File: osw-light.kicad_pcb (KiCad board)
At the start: 2 copper layers, 34.9 x 36.2 mm, 56 parts, among them J1 Conn_01x02, J2 USB_C_Receptacle_USB2.0, J3 Conn_01x02, J4 Conn_01x04, J5 Conn_01x04, Q1 2N7002, SW1 SW_Push, SW2 SW_Push, SW4 SW_Push, SW5 SW_Push, U1 DS3231MZ, U10 XC6209, U11 MCP73831T-2ACI_OT, U13 XC6209, U2 BMA400, U4 GC9A01_IPS_display, U6 CH340E, U7 ttgo-32-micro, U9 TPS2115A

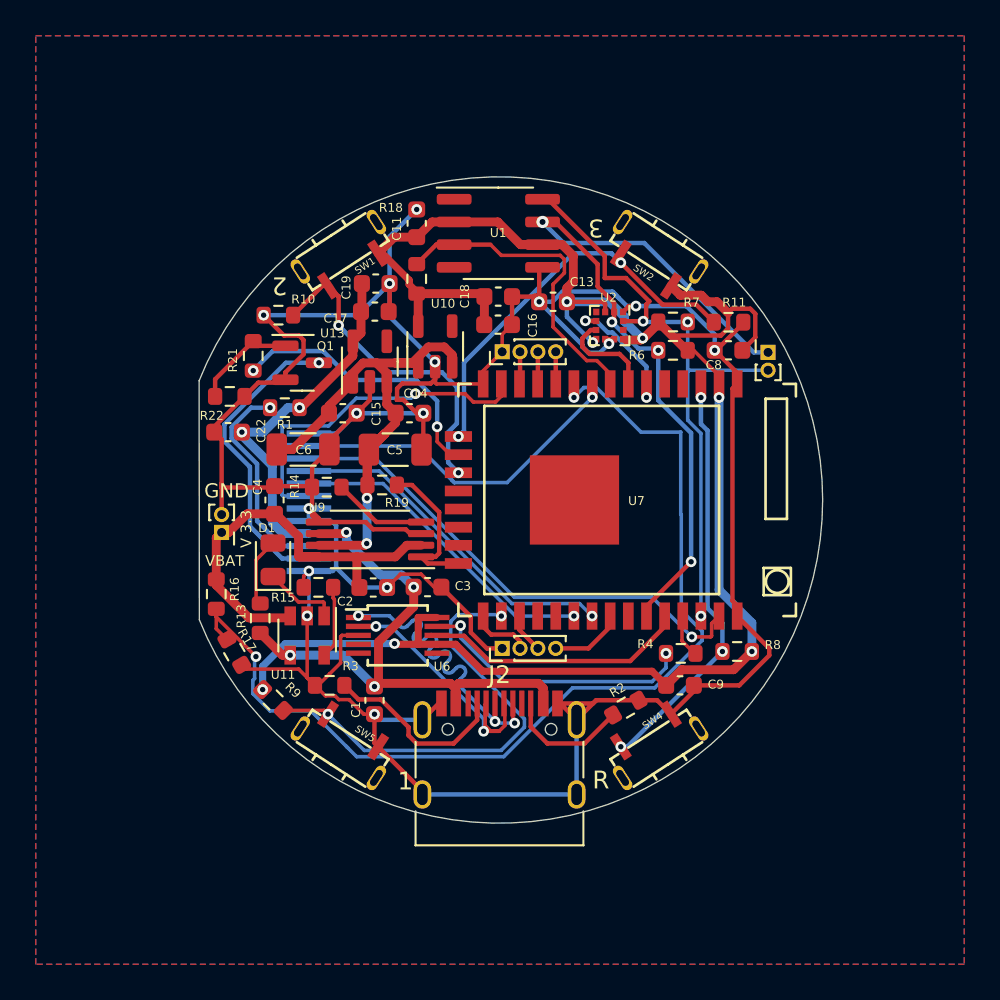
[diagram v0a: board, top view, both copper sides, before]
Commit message: re-thought some aspects of the pcb and schematics: now there is only one ldo and pcb layout is now better for hand soldering, still needs some cleanup (and bom consolidation)
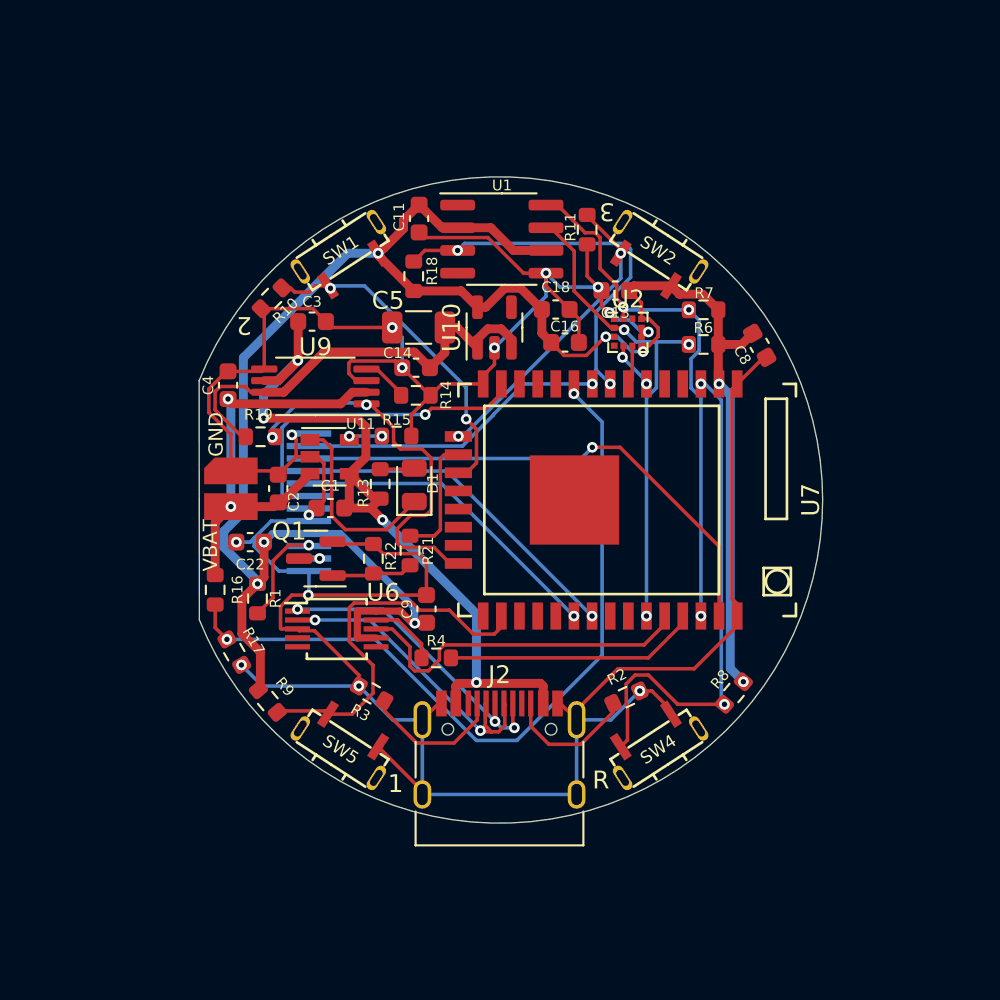
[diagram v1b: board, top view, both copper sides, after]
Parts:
- removed C15, C19: 0.1u, Capacitor_SMD:C_0603_1608Metric
- removed C17: 4.7u, Capacitor_SMD:C_0603_1608Metric
- removed C6: 100u, Capacitor_SMD:C_1206_3216Metric
- removed J3: Conn_01x02, open-Smartwatch:PinHeader_1x02_P1.0mm_Vertical
- removed J4, J5: Conn_01x04, open-Smartwatch:PinHeader_1x04_P1.00mm_Vertical
- removed U13: XC6209, Package_TO_SOT_SMD:SOT-23-5
- J1: footprint open-Smartwatch:PinHeader_1x02_P1.0mm_Vertical -> open-Smartwatch:batteryPads
- moved C3 16.2 mm to (58.5, 102.0)
- moved C9 14.8 mm to (64.9, 118.1), turned to 90 degrees
- moved R21 14.0 mm to (64.0, 114.8), turned to 90 degrees
- moved R4 13.7 mm to (65.4, 120.8)
- moved R22 12.1 mm to (61.9, 115.3), turned to -90 degrees
- moved C1 11.0 mm to (59.5, 112.5), turned to 0 degrees
- moved Q1 11.0 mm to (58.7, 115.3), turned to 180 degrees
- moved R1 10.8 mm to (55.4, 117.5), turned to -90 degrees
- moved U11 10.1 mm to (59.5, 109.6), turned to 0 degrees
- moved R13 10.1 mm to (62.3, 111.1)
- moved R15 9.53 mm to (63.2, 108.4), turned to 0 degrees
- moved R11 9.46 mm to (73.9, 96.9), turned to -90 degrees
- moved U9 9.10 mm to (58.7, 105.6)
- moved D1 8.95 mm to (64.2, 111.2)
- moved C2 7.68 mm to (56.6, 111.4), turned to 90 degrees
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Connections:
- net /VBUS renamed VBUS
- net /VCC renamed VCC
- net Net-(D1-Pad1) renamed /STAT
- net Net-(Q1-Pad1) renamed /GATE
- net Net-(R1-Pad2) renamed /LEDA
- net Net-(R14-Pad1) renamed /ILIM
- net Net-(R15-Pad1) renamed /PROG
- C22 pad 1: /3V3_2 -> +3V3
- J1 pad 1: /VBAT -> GND
- J1 pad 2: GND -> /VBAT
- R1 pad 1: /3V3_2 -> +3V3
- U4 pad 4: /3V3_2 -> +3V3
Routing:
- net /3V3_2: track 20.3 -> 0.00 mm, vias 2 -> 0
- net GND: track 202.4 -> 182.1 mm, vias 15 -> 14
- net /SDA: track 43.9 -> 27.6 mm, vias 4 -> 3
- net /LEDK: track 17.1 -> 1.15 mm
- net /B_MON: track 57.3 -> 42.9 mm
- net /STAT_PWR: track 8.63 -> 21.9 mm, vias 0 -> 2
- net Net-(R4-Pad1): track 15.7 -> 3.89 mm, vias 2 -> 0
- net /TX: track 2.48 -> 14.2 mm
- net VCC: track 36.7 -> 25.2 mm, vias 2 -> 0
- net +3V3: track 107.8 -> 117.9 mm, vias 7 -> 8
- net VBUS: track 33.5 -> 43.3 mm
- net /PIN_LED: track 15.7 -> 6.93 mm, vias 2 -> 0
- net /STAT: track 4.20 -> 10.8 mm
- net /LEDA: track 11.9 -> 5.67 mm
- net /BTN3: track 22.4 -> 17.0 mm
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- removed copper zone on B.Cu, net GND
- removed copper zone on F.Cu, net GND
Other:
- board text removed: "GND"
- board text removed: "V 3.3"
- board text removed: "VBAT"

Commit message: pcb cleanup
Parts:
- R16: value 200k -> 210k
- R19: value 220k -> 210k
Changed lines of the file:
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@@
       (effects (font (size 0.6 0.6) (thickness 0.09)))
     )
-    (fp_text value "220k" (at 0 1.43) (layer "F.Fab")
+    (fp_text value "210k" (at 0 1.43) (layer "F.Fab")
       (effects (font (size 1 1) (thickness 0.15)))
     )
@@
     (property "Sheetname" "")
     (attr smd)
-    (fp_text reference "R13" (at 0.51 0.94 -90) (layer "F.SilkS")
+    (fp_text reference "R13" (at 0.68 0.95 -90) (layer "F.SilkS")
       (effects (font (size 0.6 0.6) (thickness 0.09)))
     )
@@
     (property "Sheetname" "")
     (attr smd)
-    (fp_text reference "U10" (at 0 -2.4 90) (layer "F.SilkS")
-      (effects (font (size 1 1) (thickness 0.15)))
+    (fp_text reference "U10" (at 1.91 -2.02) (layer "F.SilkS")
+      (effects (font (size 0.6 0.6) (thickness 0.09)))
     )
     (fp_text value "XC6209" (at 0 2.4 90) (layer "F.Fab")
@@
     (property "Sheetname" "")
     (attr smd)
-    (fp_text reference "C1" (at 0 -1.25) (layer "F.SilkS")
+    (fp_text reference "C1" (at -1.2 -0.81) (layer "F.SilkS")
       (effects (font (size 0.6 0.6) (thickness 0.09)))
     )
@@
     (property "Sheetname" "")
     (attr smd)
-    (fp_text reference "D1" (at 0.08 1.04 90) (layer "F.SilkS")
+    (fp_text reference "D1" (at 1.61 -1.04 90) (layer "F.SilkS")
       (effects (font (size 0.6 0.6) (thickness 0.09)))
     )
@@
       (effects (font (size 0.6 0.6) (thickness 0.09)))
     )
-    (fp_text value "200k" (at 0 1.43 -90) (layer "F.Fab")
+    (fp_text value "210k" (at 0 1.43 -90) (layer "F.Fab")
       (effects (font (size 1 1) (thickness 0.15)))
     )
@@
     (property "Sheetname" "")
     (attr smd)
-    (fp_text reference "C13" (at 0 -1.25 180) (layer "F.SilkS")
+    (fp_text reference "C13" (at 1.01 0.9 180) (layer "F.SilkS")
       (effects (font (size 0.6 0.6) (thickness 0.09)))
     )
@@
     (property "Sheetname" "")
     (attr smd)
-    (fp_text reference "U2" (at 0 -1.85) (layer "F.SilkS")
-      (effects (font (size 1 1) (thickness 0.15)))
+    (fp_text reference "U2" (at 1.08 -1.52) (layer "F.SilkS")
+      (effects (font (size 0.6 0.6) (thickness 0.09)))
     )
     (fp_text value "BMA400" (at 0 1.6) (layer "F.Fab")

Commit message: wow ive did something
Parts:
- R16: value 210k -> 200k
- R19: value 210k -> 220k
- U10: value XC6209 -> XC6209F332MR-G
- moved R9 0.92 mm to (56.7, 122.7)
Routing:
- net /B_MON: track 42.9 -> 39.5 mm
- net /D_P: track 17.3 -> 19.3 mm, vias 3 -> 2
- net +3V3: track 117.9 -> 116.0 mm
- net VBUS: track 43.3 -> 45.0 mm
- net /D_N: track 17.4 -> 16.2 mm
- net GND: track 182.1 -> 182.6 mm, vias 14 -> 13
